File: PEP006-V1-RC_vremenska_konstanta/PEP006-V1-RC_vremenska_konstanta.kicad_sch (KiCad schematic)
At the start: 11 parts, among them J2 Screw_Terminal_01x02, SW1 SW_Push, SW2 SW_Push

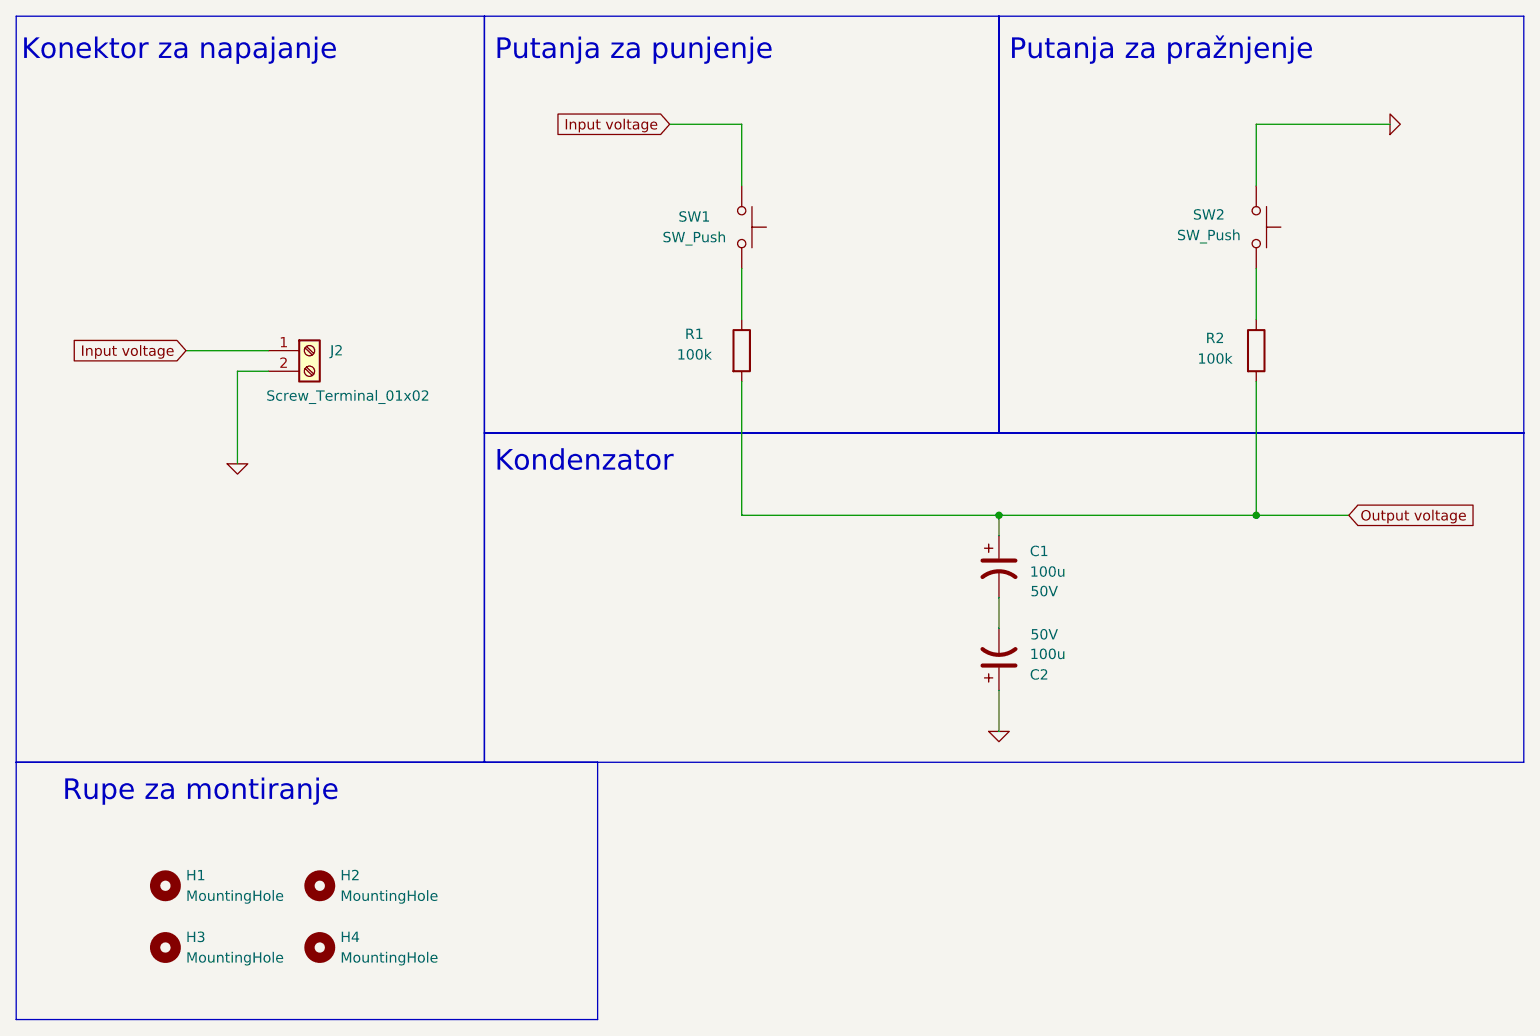
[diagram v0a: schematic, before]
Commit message: PEP006 rename.
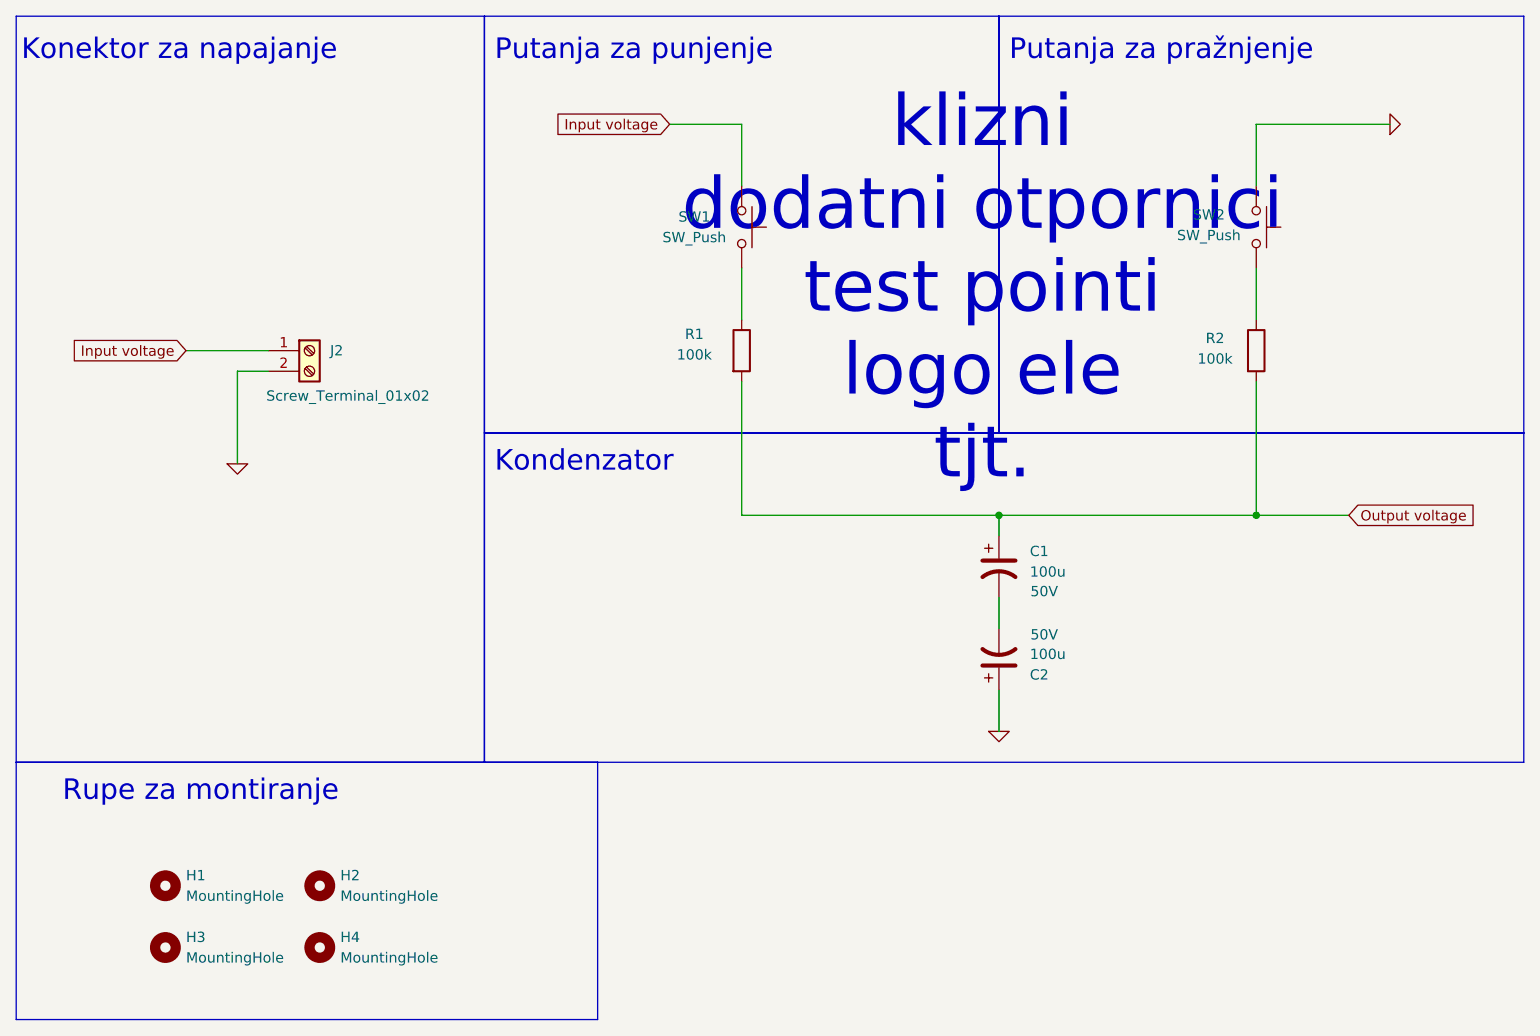
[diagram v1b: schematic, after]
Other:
- note added: "klizni dodatni otpornici test pointi logo ele tjt."
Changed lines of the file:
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@@
+		)
+	)
+	(text "klizni\ndodatni otpornici\ntest pointi\nlogo ele\ntjt."
+		(exclude_from_sim no)
+		(at 131.318 45.72 0)
+		(effects
+			(font
+				(size 6.35 6.35)
+			)
 		)
 	)
